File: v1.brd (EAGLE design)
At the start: 40.3 x 45.7 mm, 10 parts, among them J2 AVR_SPI_PROG_3X2NS, U1 ATTINY85-20S

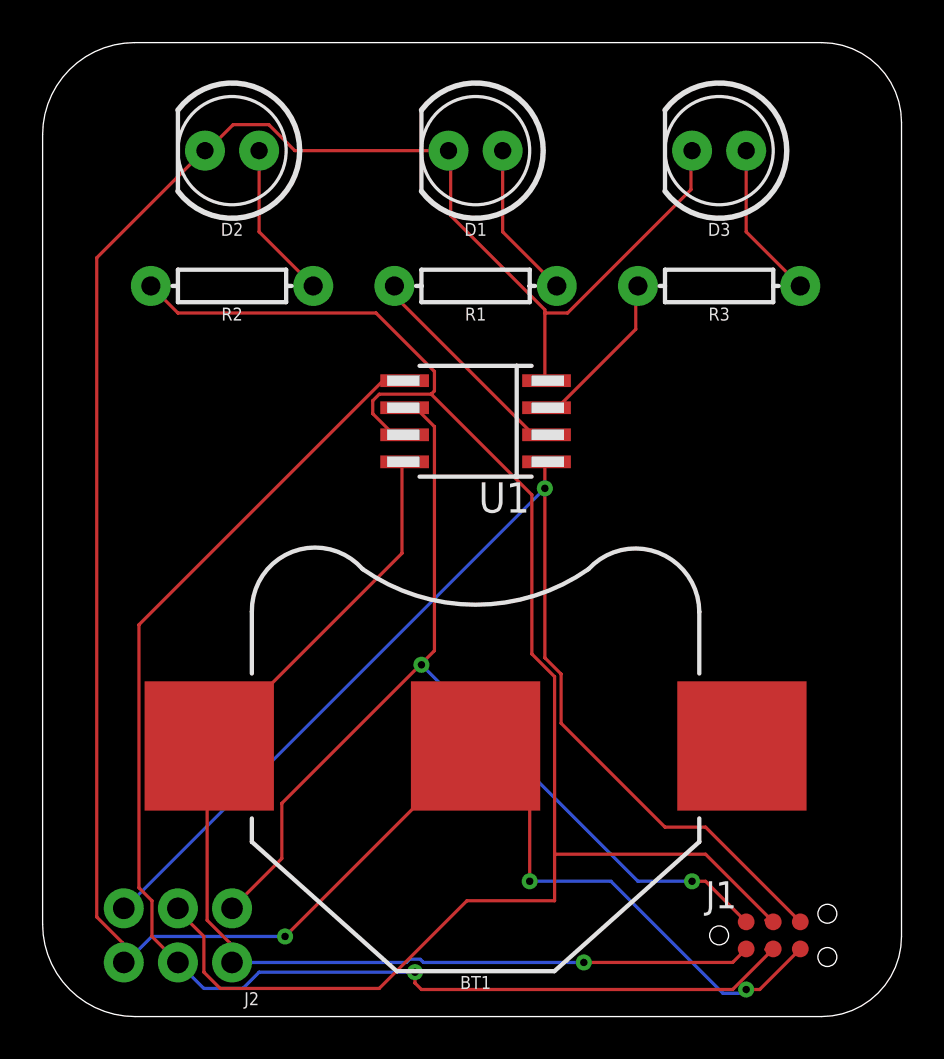
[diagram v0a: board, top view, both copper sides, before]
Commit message: corrected floating via and improved position of via in bottom right as it was to close to the miso line
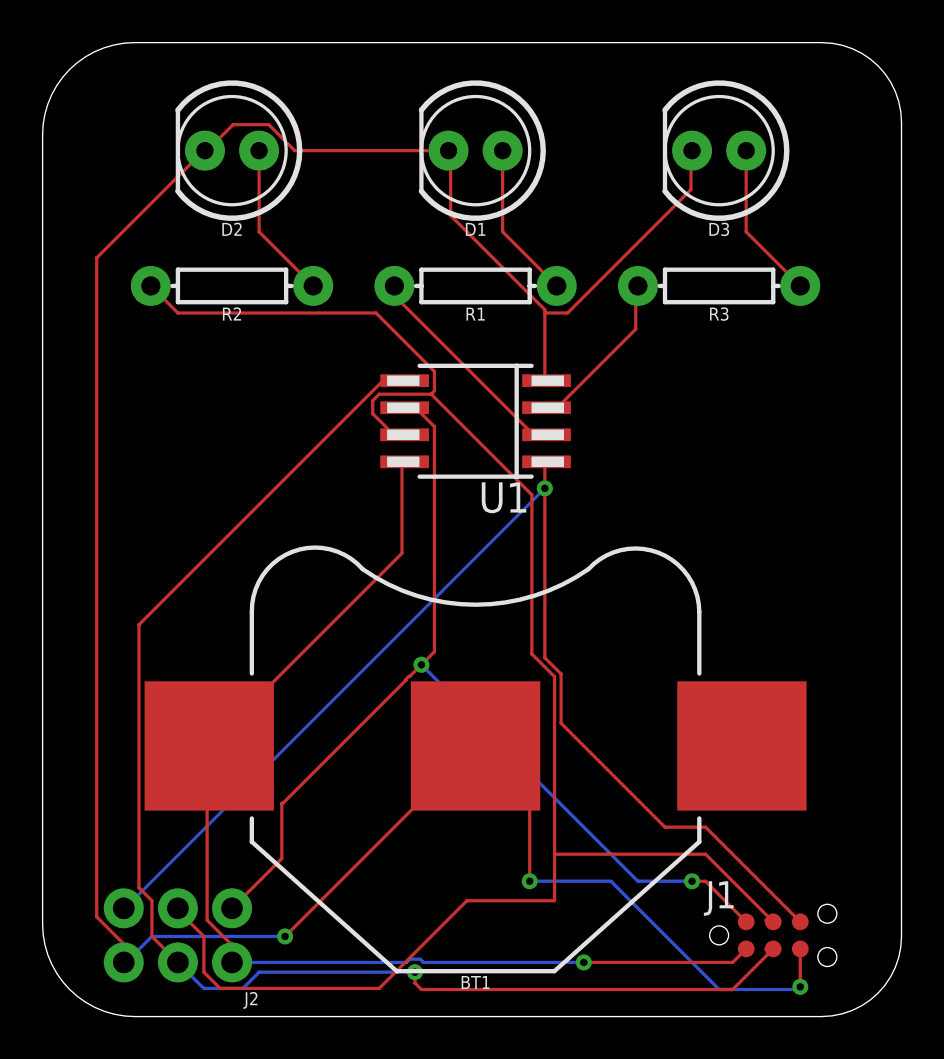
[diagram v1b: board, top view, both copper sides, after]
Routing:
- net GND: track 121.0 -> 122.1 mm, vias 2 -> 3
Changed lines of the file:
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@@
 <via x="31.75" y="15.24" extent="1-16" drill="0.35"/>
 <wire x1="31.75" y1="15.24" x2="35.56" y2="15.24" width="0.1524" layer="16"/>
-<wire x1="35.56" y1="15.24" x2="40.8178" y2="9.9822" width="0.1524" layer="16"/>
-<wire x1="40.8178" y1="9.9822" x2="41.91" y2="9.9822" width="0.1524" layer="16"/>
-<wire x1="44.45" y1="12.065" x2="42.545" y2="10.16" width="0.1524" layer="1"/>
-<wire x1="42.545" y1="10.16" x2="41.91" y2="10.16" width="0.1524" layer="1"/>
-<wire x1="41.91" y1="9.9822" x2="41.91" y2="10.16" width="0" layer="19" extent="1-16"/>
+<wire x1="35.56" y1="15.24" x2="40.64" y2="10.16" width="0.1524" layer="16"/>
+<wire x1="44.45" y1="12.065" x2="44.45" y2="10.2842" width="0.1524" layer="1"/>
+<wire x1="44.45" y1="10.2842" x2="44.45" y2="10.16" width="0.1524" layer="1"/>
+<via x="44.45" y="10.2842" extent="1-16" drill="0.35"/>
+<wire x1="40.64" y1="10.16" x2="44.3258" y2="10.16" width="0.1524" layer="16"/>
+<wire x1="44.3258" y1="10.16" x2="44.45" y2="10.2842" width="0.1524" layer="16"/>
 </signal>
 <signal name="VCC">
@@
 <contactref element="J1" pad="2"/>
 <wire x1="26.5176" y1="37.338" x2="25.908" y2="37.338" width="0.1524" layer="1"/>
-<wire x1="27.2796" y1="36.576" x2="26.5176" y2="37.338" width="0.1524" layer="1"/>
-<wire x1="27.2796" y1="26.0604" x2="27.2796" y2="36.576" width="0.1524" layer="1"/>
-<wire x1="20.1168" y1="18.8976" x2="27.2796" y2="26.0604" width="0.1524" layer="1"/>
-<wire x1="20.1168" y1="16.3068" x2="20.1168" y2="18.8976" width="0.1524" layer="1"/>
+<wire x1="26.5176" y1="37.338" x2="27.2796" y2="36.576" width="0.1524" layer="1"/>
+<wire x1="20.1168" y1="18.8976" x2="20.1168" y2="16.3068" width="0.1524" layer="1"/>
 <wire x1="17.78" y1="13.97" x2="20.1168" y2="16.3068" width="0.1524" layer="1"/>
 <wire x1="25.908" y1="37.338" x2="25.88" y2="37.465" width="0.1524" layer="1"/>
-<wire x1="26.67" y1="25.4" x2="26.6446" y2="25.4254" width="0" layer="19" extent="1-1"/>
 <wire x1="41.91" y1="13.335" x2="40.005" y2="15.24" width="0.1524" layer="1"/>
 <wire x1="40.005" y1="15.24" x2="39.37" y2="15.24" width="0.1524" layer="1"/>
@@
 <wire x1="36.83" y1="15.24" x2="26.67" y2="25.4" width="0.1524" layer="16"/>
 <via x="26.67" y="25.4" extent="1-16" drill="0.35"/>
+<wire x1="27.2796" y1="26.0096" x2="26.67" y2="25.4" width="0.1524" layer="1"/>
+<wire x1="27.2796" y1="36.576" x2="27.2796" y2="26.0096" width="0.1524" layer="1"/>
+<wire x1="20.1676" y1="18.8976" x2="20.1168" y2="18.8976" width="0.1524" layer="1"/>
+<wire x1="26.67" y1="25.4" x2="26.1236" y2="24.8536" width="0.1524" layer="1"/>
+<wire x1="26.1236" y1="24.8536" x2="26.0803125" y2="24.8536" width="0.1524" layer="1"/>
+<wire x1="26.0803125" y1="24.8536" x2="25.9464" y2="24.7196875" width="0.1524" layer="1"/>
+<wire x1="25.9464" y1="24.7196875" x2="25.9464" y2="24.6764" width="0.1524" layer="1"/>
+<wire x1="25.9464" y1="24.6764" x2="20.1676" y2="18.8976" width="0.1524" layer="1"/>
 </signal>
 <signal name="MOSI">
@@
 <wire x1="40.005" y1="16.51" x2="32.9184" y2="16.51" width="0.1524" layer="1"/>
 </signal>
-<signal name="N$2">
-<via x="41.91" y="10.16" extent="1-16" drill="0.35"/>
-</signal>
 </signals>

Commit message: moved battery to layer 2 and cleaned up tracks
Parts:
- flipped BT1 to the bottom
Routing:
- net VCC: track 52.4 -> 77.0 mm, vias 1 -> 2
- net GND: track 122.1 -> 127.8 mm, vias 3 -> 4
- net MISO: track 48.7 -> 51.5 mm
- net MOSI: track 64.4 -> 63.6 mm
- net A1: track 81.6 -> 80.9 mm
- net RST: track 55.6 -> 55.2 mm, vias 1 -> 2
